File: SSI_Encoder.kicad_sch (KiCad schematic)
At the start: 36 parts, among them J2 DE9_Socket_MountingHoles, J4 DE9_Socket_MountingHoles, Q6 2N7002KQ-7, Q7 2N7002KQ-7, U16 ISO1432DWR, U22 SN74LVC2G07DCKR(UMW), U26 TPD1E10B09DPYR, U27 TPD1E10B09DPYR, U3 TPD2E2U06QDBZRQ1, U6 TPD2E2U06QDBZRQ1, U7 ISO1432DWR, U8 TPD2E2U06QDBZRQ1, U9 TPD2E2U06QDBZRQ1

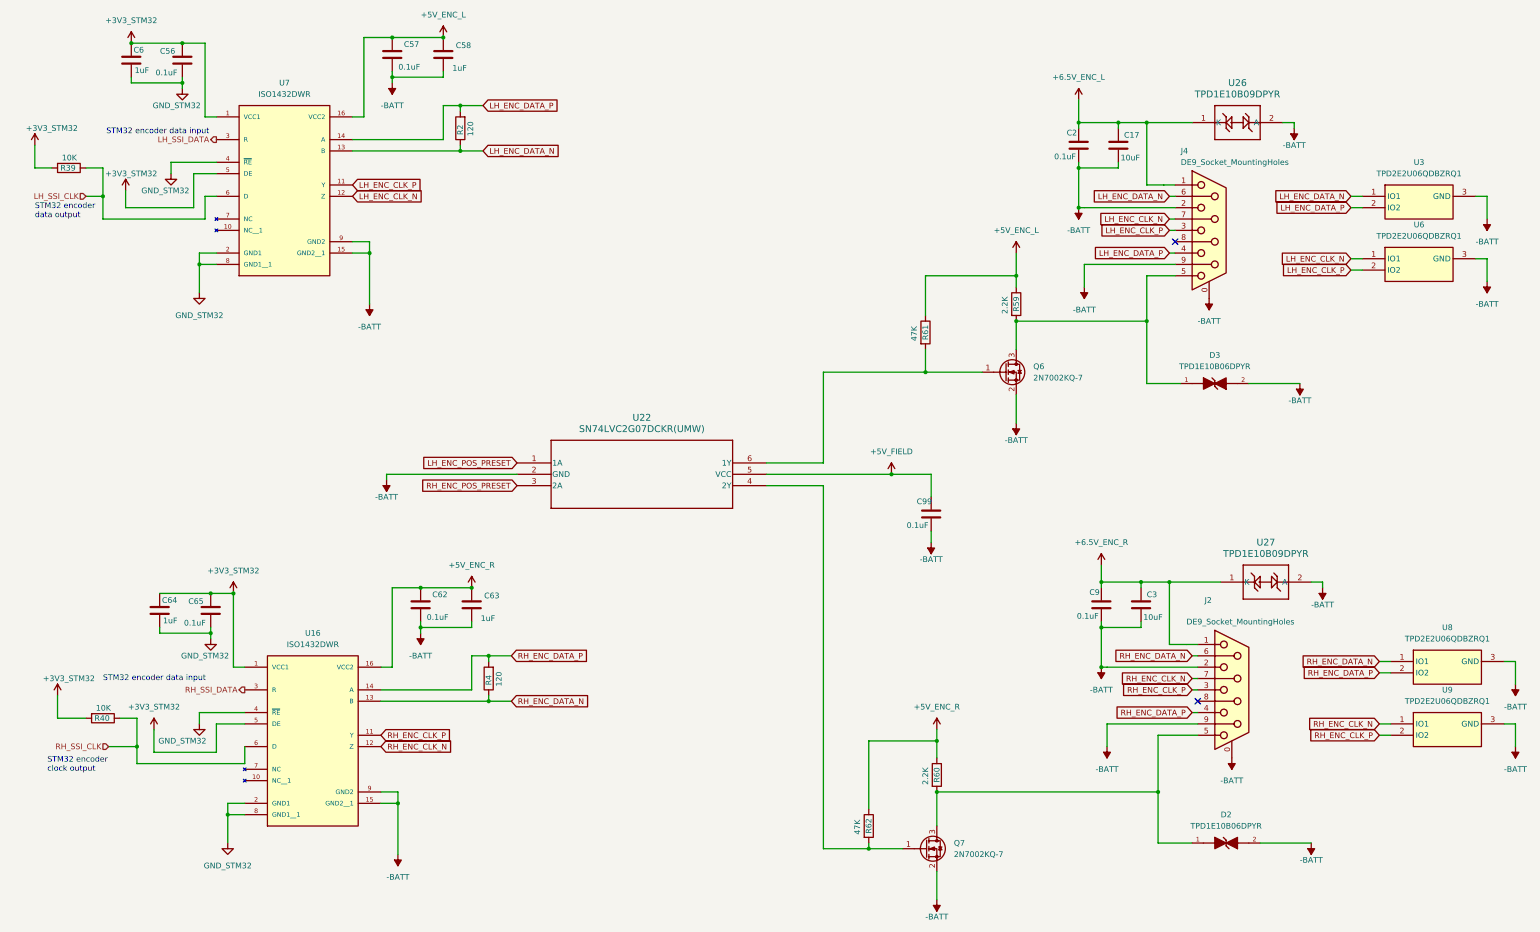
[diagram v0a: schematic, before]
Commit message: Redesign schematic for dual motor encoders
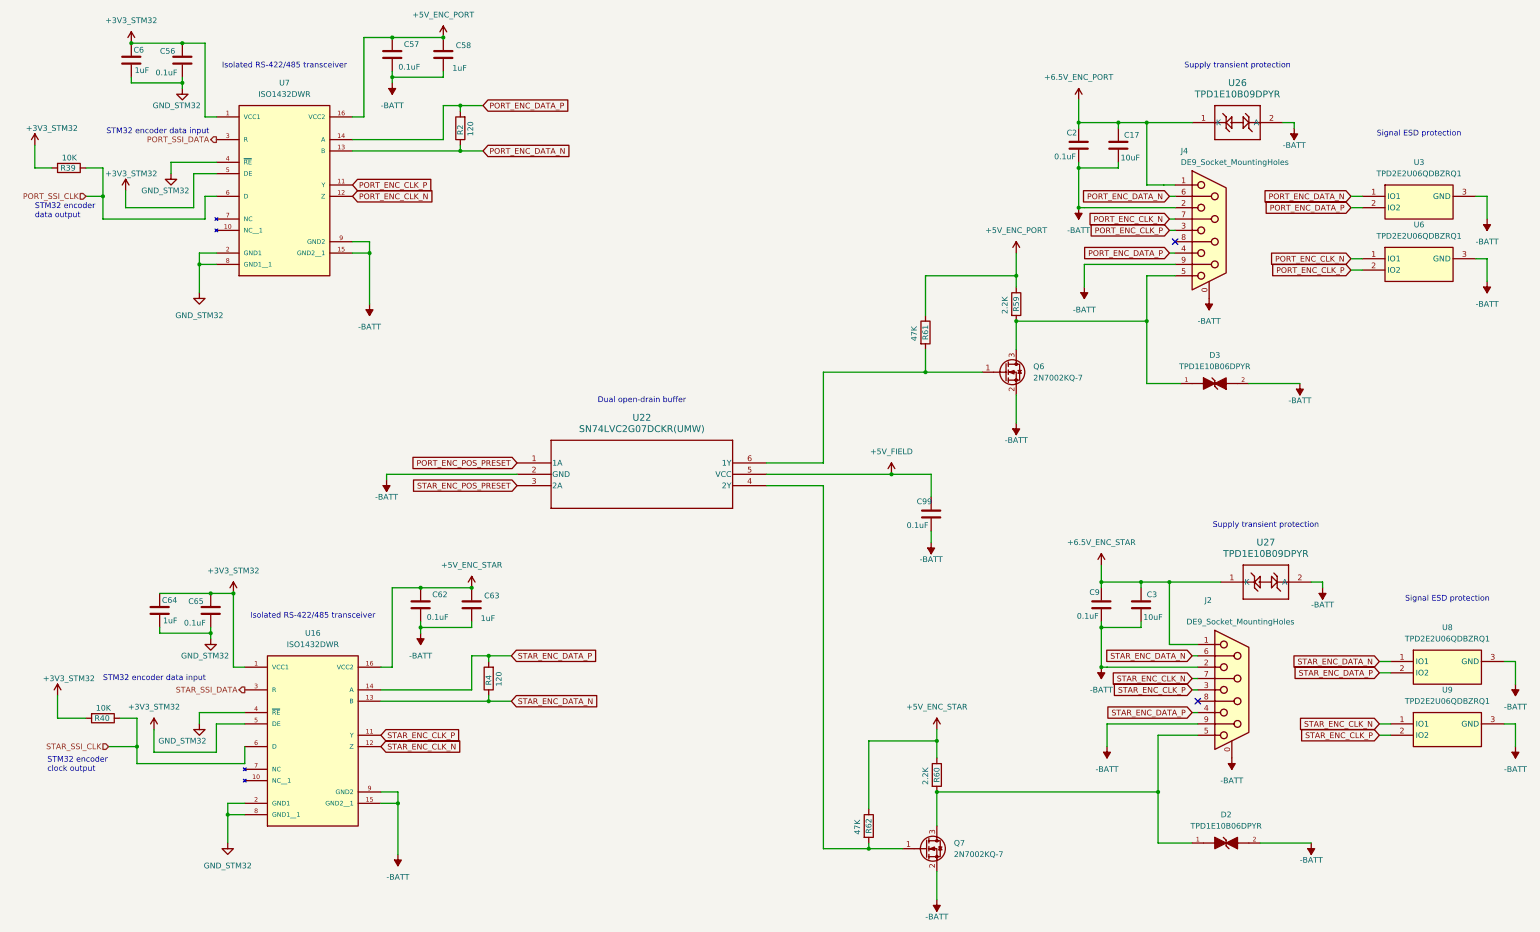
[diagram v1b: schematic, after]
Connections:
- net +5V_ENC_L renamed +5V_ENC_PORT
- net +5V_ENC_R renamed +5V_ENC_STAR
- net +6.5V_ENC_L renamed +6.5V_ENC_PORT
- net +6.5V_ENC_R renamed +6.5V_ENC_STAR
- net LH_ENC_CLK_N renamed PORT_ENC_CLK_N
- net LH_ENC_CLK_P renamed PORT_ENC_CLK_P
- net LH_ENC_DATA_N renamed PORT_ENC_DATA_N
- net LH_ENC_DATA_P renamed PORT_ENC_DATA_P
- net LH_ENC_POS_PRESET renamed PORT_ENC_POS_PRESET
- net LH_SSI_CLK renamed PORT_SSI_CLK
- net LH_SSI_DATA renamed PORT_SSI_DATA
- net RH_ENC_CLK_N renamed STAR_ENC_CLK_N
- net RH_ENC_CLK_P renamed STAR_ENC_CLK_P
- net RH_ENC_DATA_N renamed STAR_ENC_DATA_N
- net RH_ENC_DATA_P renamed STAR_ENC_DATA_P
- net RH_ENC_POS_PRESET renamed STAR_ENC_POS_PRESET
- net RH_SSI_CLK renamed STAR_SSI_CLK
- net RH_SSI_DATA renamed STAR_SSI_DATA
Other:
- note added: "Dual open-drain buffer"
- note added: "Isolated RS-422/485 transceiver"
- note added: "Signal ESD protection"
- note added: "Supply transient protection"
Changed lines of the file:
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@@
 	(title_block
 		(title "Elevation Control_Gigabit")
-		(date "2026-09-01")
-		(rev "Sep_2026_V1")
+		(date "2026-10-03")
+		(rev "P3 REVIEW")
 		(company "Starspec")
 		(comment 4 "Mauro M. Coutinho")
@@
 		)
 	)
+	(text "Isolated RS-422/485 transceiver"
+		(exclude_from_sim no)
+		(at 90.17 39.37 0)
+		(effects
+			(font
+				(size 1.27 1.27)
+			)
+		)
+	)
+	(text "Signal ESD protection"
+		(exclude_from_sim no)
+		(at 350.52 158.75 0)
+		(effects
+			(font
+				(size 1.27 1.27)
+			)
+		)
+	)
+	(text "Supply transient protection"
+		(exclude_from_sim no)
+		(at 309.88 142.24 0)
+		(effects
+			(font
+				(size 1.27 1.27)
+			)
+		)
+	)
+	(text "Signal ESD protection"
+		(exclude_from_sim no)
+		(at 344.17 54.61 0)
+		(effects
+			(font
+				(size 1.27 1.27)
+			)
+		)
+	)
+	(text "Supply transient protection"
+		(exclude_from_sim no)
+		(at 303.53 39.37 0)
+		(effects
+			(font
+				(size 1.27 1.27)
+			)
+		)
+	)
 	(text "STM32 encoder data input"
 		(exclude_from_sim no)
@@
 		)
 	)
+	(text "Isolated RS-422/485 transceiver"
+		(exclude_from_sim no)
+		(at 96.52 162.56 0)
+		(effects
+			(font
+				(size 1.27 1.27)
+			)
+		)
+	)
 	(text "STM32 encoder \nclock output"
 		(exclude_from_sim no)
@@
 		)
 	)
+	(text "Dual open-drain buffer"
+		(exclude_from_sim no)
+		(at 170.18 114.3 0)
+		(effects
+			(font
+				(size 1.27 1.27)
+			)
+		)
+	)
 	(text "STM32 encoder data input"
 		(exclude_from_sim no)
@@
 		)
 	)
-	(global_label "RH_ENC_DATA_N"
+	(global_label "STAR_ENC_DATA_N"
 		(shape input)
 		(at 140.97 181.61 0)
@@
 		)
 	)
-	(global_label "RH_ENC_CLK_P"
+	(global_label "STAR_ENC_CLK_P"
 		(shape input)
 		(at 335.28 189.23 180)
@@
 		)
 	)
-	(global_label "LH_ENC_DATA_N"
+	(global_label "PORT_ENC_DATA_N"
 		(shape input)
 		(at 288.29 68.58 180)
@@
 		)
 	)
-	(global_label "RH_ENC_POS_PRESET"
+	(global_label "STAR_ENC_POS_PRESET"
 		(shape input)
 		(at 142.24 133.35 180)
@@
 		)
 	)
-	(global_label "LH_ENC_CLK_P"
+	(global_label "PORT_ENC_CLK_P"
 		(shape input)
 		(at 288.29 76.2 180)
@@
 		)
 	)
-	(global_label "RH_ENC_DATA_N"
+	(global_label "STAR_ENC_DATA_N"
 		(shape input)
 		(at 293.37 171.45 180)
@@
 		)
 	)
-	(global_label "RH_ENC_CLK_N"
+	(global_label "STAR_ENC_CLK_N"
 		(shape input)
 		(at 111.76 191.77 0)
@@
 		)
 	)
-	(global_label "RH_ENC_DATA_P"
+	(global_label "STAR_ENC_DATA_P"
 		(shape input)
 		(at 293.37 184.15 180)
@@
 		)
 	)
-	(global_label "RH_ENC_DATA_N"
+	(global_label "STAR_ENC_DATA_N"
 		(shape input)
 		(at 335.28 172.72 180)
@@
 		)
 	)
-	(global_label "LH_ENC_DATA_P"
+	(global_label "PORT_ENC_DATA_P"
 		(shape input)
 		(at 288.29 81.28 180)
@@
 		)
 	)
-	(global_label "RH_ENC_DATA_P"
+	(global_label "STAR_ENC_DATA_P"
 		(shape input)
 		(at 335.28 175.26 180)
@@
 		)
 	)
-	(global_label "LH_ENC_DATA_N"
+	(global_label "PORT_ENC_DATA_N"
 		(shape input)
 		(at 328.93 68.58 180)
@@
 		)
 	)
-	(global_label "LH_ENC_CLK_N"
+	(global_label "PORT_ENC_CLK_N"
 		(shape input)
 		(at 328.93 82.55 180)
@@
 		)
 	)
-	(global_label "LH_ENC_POS_PRESET"
+	(global_label "PORT_ENC_POS_PRESET"
 		(shape input)
 		(at 142.24 128.27 180)
@@
 		)
 	)
-	(global_label "LH_ENC_CLK_P"
+	(global_label "PORT_ENC_CLK_P"
 		(shape input)
 		(at 105.41 66.04 0)
@@
 		)
 	)
-	(global_label "LH_ENC_DATA_P"
+	(global_label "PORT_ENC_DATA_P"
 		(shape input)
 		(at 328.93 71.12 180)
@@
 		)
 	)
-	(global_label "RH_ENC_DATA_P"
+	(global_label "STAR_ENC_DATA_P"
 		(shape input)
 		(at 140.97 171.45 0)
@@
 		)
 	)
-	(global_label "LH_ENC_CLK_N"
+	(global_label "PORT_ENC_CLK_N"
 		(shape input)
 		(at 105.41 68.58 0)
@@
 		)
 	)
-	(global_label "RH_ENC_CLK_N"
+	(global_label "STAR_ENC_CLK_N"
 		(shape input)
 		(at 335.28 186.69 180)
@@
 		)
 	)
-	(global_label "LH_ENC_CLK_P"
+	(global_label "PORT_ENC_CLK_P"
 		(shape input)
 		(at 328.93 85.09 180)
@@
 		)
 	)
-	(global_label "LH_ENC_CLK_N"
+	(global_label "PORT_ENC_CLK_N"
 		(shape input)
 		(at 288.29 73.66 180)
@@
 		)
 	)
-	(global_label "LH_ENC_DATA_N"
+	(global_label "PORT_ENC_DATA_N"
 		(shape input)
 		(at 134.62 58.42 0)
@@
 		)
 	)
-	(global_label "RH_ENC_CLK_P"
+	(global_label "STAR_ENC_CLK_P"
 		(shape input)
 		(at 293.37 179.07 180)
@@
 		)
 	)
-	(global_label "LH_ENC_DATA_P"
+	(global_label "PORT_ENC_DATA_P"
 		(shape input)
 		(at 134.62 48.26 0)
@@
 		)
 	)
-	(global_label "RH_ENC_CLK_P"
+	(global_label "STAR_ENC_CLK_P"
 		(shape input)
 		(at 111.76 189.23 0)
@@
 		)
 	)
-	(global_label "RH_ENC_CLK_N"
+	(global_label "STAR_ENC_CLK_N"
 		(shape input)
 		(at 293.37 176.53 180)
@@
 		)
 	)
-	(hierarchical_label "LH_SSI_CLK"
+	(hierarchical_label "PORT_SSI_CLK"
 		(shape input)
 		(at 45.72 68.58 180)
@@
 		)
 	)
-	(hierarchical_label "RH_SSI_DATA"
+	(hierarchical_label "STAR_SSI_DATA"
 		(shape output)
 		(at 81.28 179.07 180)
@@
 		)
 	)
-	(hierarchical_label "RH_SSI_CLK"
+	(hierarchical_label "STAR_SSI_CLK"
 		(shape input)
 		(at 50.8 191.77 180)
@@
 		)
 	)
-	(hierarchical_label "LH_SSI_DATA"
+	(hierarchical_label "PORT_SSI_DATA"
 		(shape output)
 		(at 74.93 55.88 180)
@@
 	)
 	(symbol
-		(lib_id "Power_Custom:+5V_ENC_L")
+		(lib_id "Power_Custom:+5V_ENC_PORT")
 		(at 125.73 33.02 0)
 		(unit 1)
@@
 			)
 		)
-		(property "Value" "+5V_ENC_L"
+		(property "Value" "+5V_ENC_PORT"
 			(at 125.73 27.94 0)
 			(effects
@@
 	)
 	(symbol
-		(lib_id "Power_Custom:+5V_ENC_R")
+		(lib_id "Power_Custom:+5V_ENC_STAR")
 		(at 236.22 187.96 0)
 		(unit 1)
@@
 			)
 		)
-		(property "Value" "+5V_ENC_R"
+		(property "Value" "+5V_ENC_STAR"
 			(at 236.22 182.88 0)
 			(effects
@@
 		(property "ALT_LCSC" "C2860423"
 			(at 142.24 128.27 0)
-			(effects (font (size 1.27 1.27)) (hide yes))
+			(effects
+				(font
+					(size 1.27 1.27)
+				)
+				(hide yes)
+			)
 		)
 		(property "ALT_MANUFACTURER_PART_NUMBER" "SN74LVC2G07MDCKTEP"
 			(at 142.24 128.27 0)
-			(effects (font (size 1.27 1.27)) (hide yes))
+			(effects
+				(font
+					(size 1.27 1.27)
+				)
+				(hide yes)
+			)
 		)
 		(pin "1"
@@
 	)
 	(symbol
-		(lib_id "Power_Custom:6.5V_ENC_L")
+		(lib_id "Power_Custom:6.5V_ENC_PORT")
 		(at 267.97 46.99 0)
 		(unit 1)
@@
 			)
 		)
-		(property "Value" "+6.5V_ENC_L"
+		(property "Value" "+6.5V_ENC_PORT"
 			(at 267.97 41.91 0)
 			(effects
@@
 	)
 	(symbol
-		(lib_id "Power_Custom:+5V_ENC_L")
+		(lib_id "Power_Custom:+5V_ENC_PORT")
 		(at 254 81.28 0)
 		(unit 1)
@@
 			)
 		)
-		(property "Value" "+5V_ENC_L"
+		(property "Value" "+5V_ENC_PORT"
 			(at 254 76.2 0)
 			(effects
@@
 	)
 	(symbol
-		(lib_id "Power_Custom:+5V_ENC_R")
+		(lib_id "Power_Custom:+5V_ENC_STAR")
 		(at 132.08 156.21 0)
 		(unit 1)
@@
 			)
 		)
-		(property "Value" "+5V_ENC_R"
+		(property "Value" "+5V_ENC_STAR"
 			(at 132.08 151.13 0)
 			(effects
@@
 	)
 	(symbol
-		(lib_id "Power_Custom:6.5V_ENC_L")
+		(lib_id "Power_Custom:6.5V_ENC_PORT")
 		(at 273.05 151.13 0)
 		(unit 1)
@@
 			)
 		)
-		(property "Value" "+6.5V_ENC_R"
+		(property "Value" "+6.5V_ENC_STAR"
 			(at 273.05 146.05 0)
 			(effects
